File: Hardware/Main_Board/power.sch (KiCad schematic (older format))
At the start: 5 parts

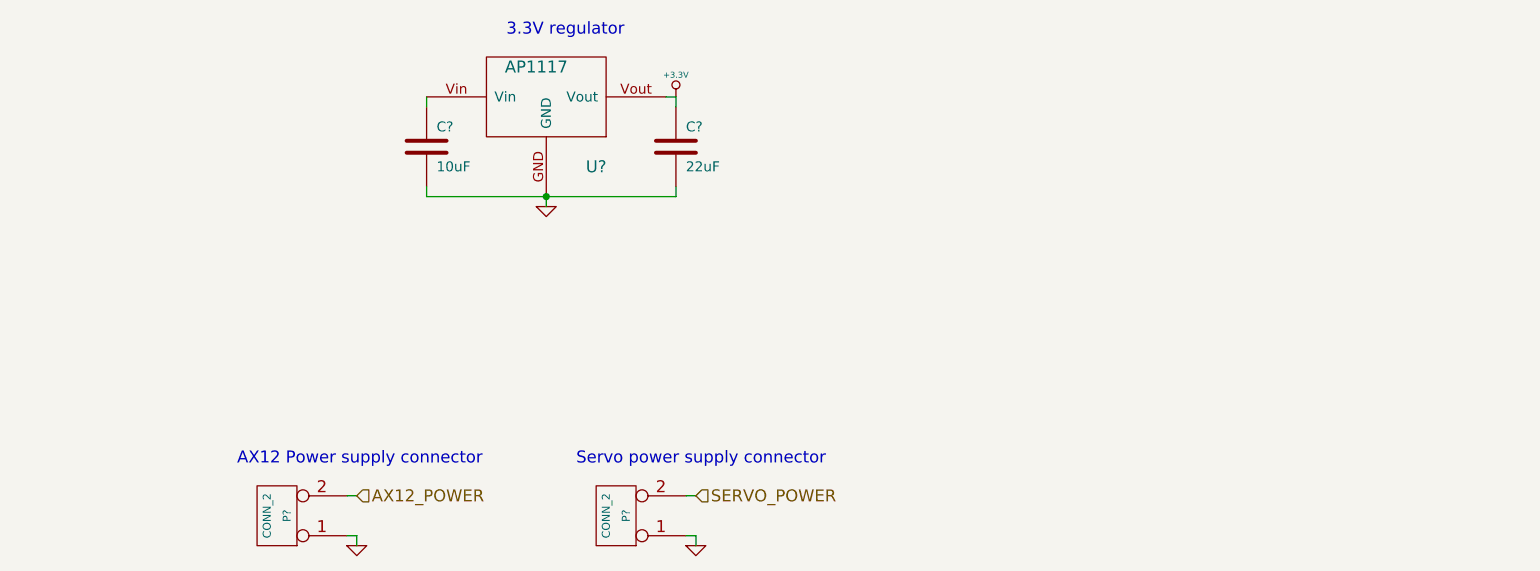
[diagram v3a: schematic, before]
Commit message: [HARDWARE] Finish motor interface and add SWD interface
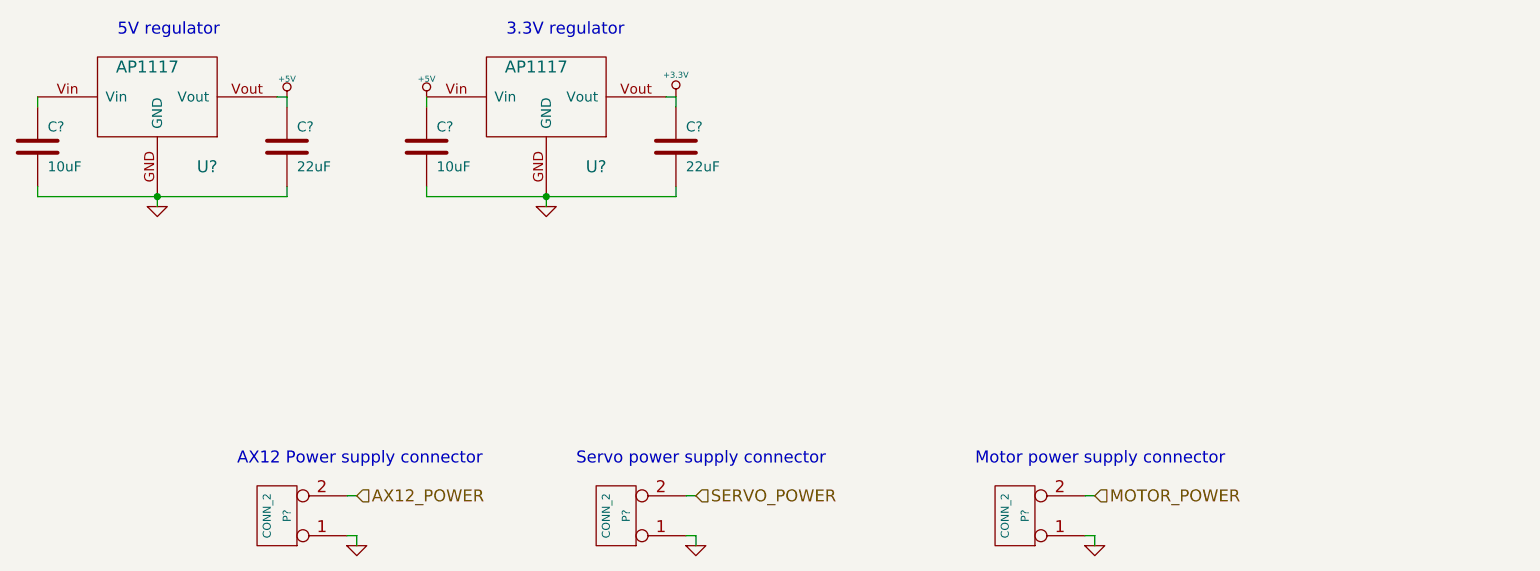
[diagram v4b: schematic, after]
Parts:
- added C?: 10uF, symbol C
- added C?: 22uF, symbol C
- added P?: CONN_2, symbol CONN_2
- added U?: AP1117, symbol AP1117
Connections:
- net GND: now also C?.2, C?.2, P?.1 (P1), U?.GND
- net +5V: now reaches C?.1, U?.Vin
- net +5V: now also C?.1, U?.Vout
- new net: C?.1, U?.Vin
- new net MOTOR_POWER: P?.2 (PM)
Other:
- note added: "5V regulator"
- note added: "Motor power supply connector"
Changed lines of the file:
@@
-EESchema Schematic File Version 2  date mer. 09 oct. 2013 08:53:10 CEST
+EESchema Schematic File Version 2  date mer. 09 oct. 2013 21:01:20 CEST
 LIBS:power
 LIBS:device
@@
 LIBS:sd_holder
 LIBS:ap1117
+LIBS:l298
 LIBS:ausbee-cache
 EELAYER 25  0
@@
 $Descr A4 11700 8267
 encoding utf-8
-Sheet 2 5
+Sheet 4 6
 Title ""
 Date "9 oct 2013"
@@
 Comment4 ""
 $EndDescr
+Text Notes 6250 4650 0    60   ~ 0
+Motor power supply connector
+Wire Wire Line
+	6850 4800 6800 4800
+Wire Wire Line
+	6850 5050 6850 5000
+Wire Wire Line
+	6850 5000 6800 5000
+Text HLabel 6850 4800 2    60   Input ~ 0
+MOTOR_POWER
+$Comp
+L GND #PWR?
+U 1 1 52558D99
+P 6850 5050
+F 0 "#PWR?" H 6850 5050 30  0001 C CNN
+F 1 "GND" H 6850 4980 30  0001 C CNN
+	1    6850 5050
+	1    0    0    -1
+$EndComp
 $Comp
 L CONN_2 P?
+U 1 1 52558D98
+P 6450 4900
+F 0 "P?" V 6400 4900 40  0000 C CNN
+F 1 "CONN_2" V 6500 4900 40  0000 C CNN
+	1    6450 4900
+	-1   0    0    1
+$EndComp
+$Comp
+L +5V #PWR?
+U 1 1 52553DBF
+P 3500 2800
+F 0 "#PWR?" H 3500 2890 20  0001 C CNN
+F 1 "+5V" H 3500 2890 30  0000 C CNN
+	1    3500 2800
+	1    0    0    -1
+$EndComp
+$Comp
+L +5V #PWR?
+U 1 1 52553DB8
+P 2800 2800
+F 0 "#PWR?" H 2800 2890 20  0001 C CNN
+F 1 "+5V" H 2800 2890 30  0000 C CNN
+	1    2800 2800
+	1    0    0    -1
+$EndComp
+$Comp
+L AP1117 U?
+U 1 1 52553DB6
+P 2150 2800
+F 0 "U?" H 2400 2450 60  0000 C CNN
+F 1 "AP1117" H 2100 2950 60  0000 C CNN
+	1    2150 2800
+	1    0    0    -1
+$EndComp
+$Comp
+L GND #PWR?
+U 1 1 52553DB4
+P 2150 3350
+F 0 "#PWR?" H 2150 3350 30  0001 C CNN
+F 1 "GND" H 2150 3280 30  0001 C CNN
+	1    2150 3350
+	1    0    0    -1
+$EndComp
+$Comp
+L C C?
+U 1 1 52553DB3
+P 2800 3050
+F 0 "C?" H 2850 3150 50  0000 L CNN
+F 1 "22uF" H 2850 2950 50  0000 L CNN
+	1    2800 3050
+	1    0    0    -1
+$EndComp
+$Comp
+L C C?
+U 1 1 52553DB2
+P 1550 3050
+F 0 "C?" H 1600 3150 50  0000 L CNN
+F 1 "10uF" H 1600 2950 50  0000 L CNN
+	1    1550 3050
+	1    0    0    -1
+$EndComp
+Text Notes 1950 2500 0    60   ~ 0
+5V regulator
+Connection ~ 2150 3300
+Wire Wire Line
+	1550 3300 1550 3250
+Wire Wire Line
+	2800 3300 1550 3300
+Wire Wire Line
+	2800 2800 2800 2850
+Wire Wire Line
+	2750 2800 2800 2800
+Wire Wire Line
+	2150 3300 2150 3350
+Wire Wire Line
+	2800 3250 2800 3300
+Wire Wire Line
+	1550 2850 1550 2800
+$Comp
+L CONN_2 P?

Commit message: [HARDWARE] Complete the SWD design, remove two undrived motor interfaces
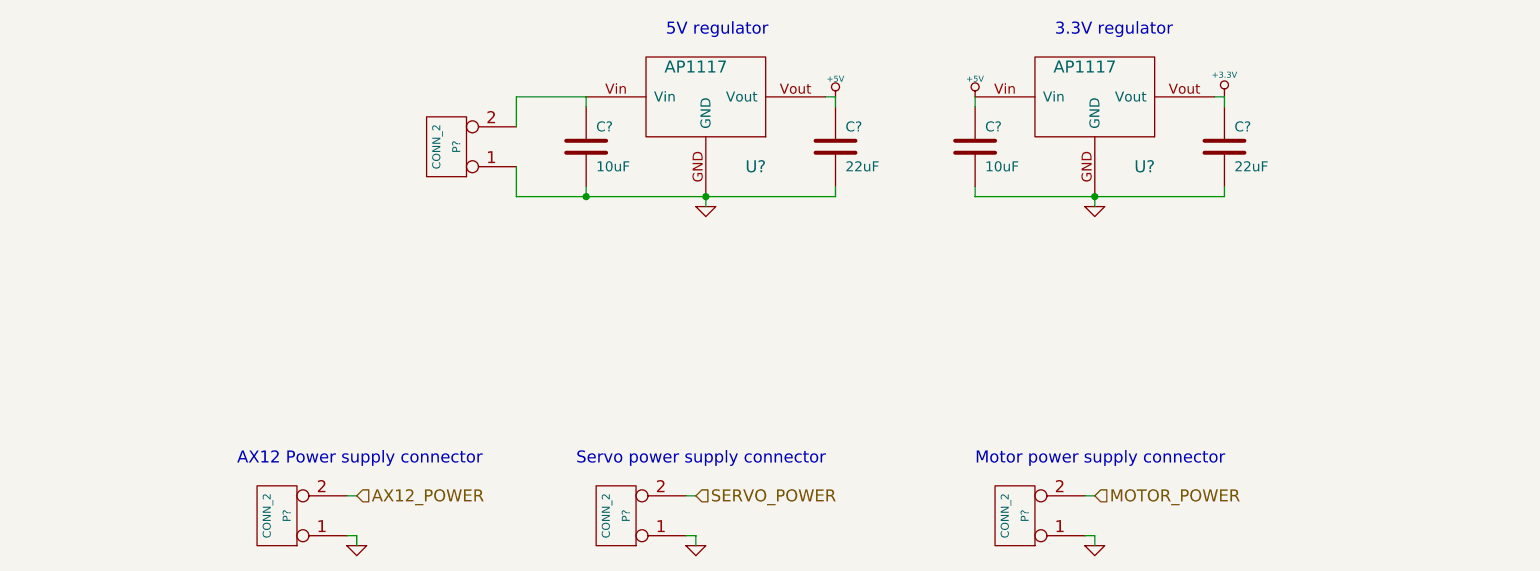
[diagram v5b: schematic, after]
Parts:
- added P?: CONN_2, symbol CONN_2
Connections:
- net GND: now also P?.1 (P1)
- net at C?.1, U?.Vin: now also P?.2 (PM)
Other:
- moved on the sheet: C?, U?
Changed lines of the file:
@@
-EESchema Schematic File Version 2  date mer. 09 oct. 2013 21:01:20 CEST
+EESchema Schematic File Version 2  date jeu. 10 oct. 2013 13:52:33 CEST
 LIBS:power
 LIBS:device
@@
 Sheet 4 6
 Title ""
-Date "9 oct 2013"
+Date "10 oct 2013"
 Rev ""
 Comp ""
@@
 Comment4 ""
 $EndDescr
+Connection ~ 4300 3300
+Wire Wire Line
+	3950 3300 5550 3300
+Wire Wire Line
+	3950 3300 3950 3150
+Wire Wire Line
+	6850 4800 6800 4800
+Wire Wire Line
+	6850 5050 6850 5000
+Wire Wire Line
+	6850 5000 6800 5000
+Connection ~ 4900 3300
+Wire Wire Line
+	4300 3300 4300 3250
+Wire Wire Line
+	5550 2850 5550 2800
+Wire Wire Line
+	5550 2800 5500 2800
+Wire Wire Line
+	4900 3300 4900 3350
+Wire Wire Line
+	5550 3300 5550 3250
+Wire Wire Line
+	4300 2850 4300 2800
+Wire Wire Line
+	4800 5000 4850 5000
+Wire Wire Line
+	4850 5000 4850 5050
+Wire Wire Line
+	4850 4800 4800 4800
+Wire Wire Line
+	3150 4800 3100 4800
+Wire Wire Line
+	6250 2850 6250 2800
+Wire Wire Line
+	7500 3250 7500 3300
+Wire Wire Line
+	6850 3300 6850 3350
+Wire Wire Line
+	7450 2800 7500 2800
+Wire Wire Line
+	7500 2800 7500 2850
+Wire Wire Line
+	7500 3300 6250 3300
+Wire Wire Line
+	6250 3300 6250 3250
+Connection ~ 6850 3300
+Wire Wire Line
+	3150 5050 3150 5000
+Wire Wire Line
+	3150 5000 3100 5000
+Wire Wire Line
+	3950 2950 3950 2800
+Wire Wire Line
+	3950 2800 4300 2800
+$Comp
+L CONN_2 P?
+U 1 1 5256944A
+P 3600 3050
+F 0 "P?" V 3550 3050 40  0000 C CNN
+F 1 "CONN_2" V 3650 3050 40  0000 C CNN
+	1    3600 3050
+	-1   0    0    1
+$EndComp
 Text Notes 6250 4650 0    60   ~ 0
 Motor power supply connector
-Wire Wire Line
-	6850 4800 6800 4800
-Wire Wire Line
-	6850 5050 6850 5000
-Wire Wire Line
-	6850 5000 6800 5000
 Text HLabel 6850 4800 2    60   Input ~ 0
 MOTOR_POWER
@@
 L +5V #PWR?
 U 1 1 52553DBF
-P 3500 2800
-F 0 "#PWR?" H 3500 2890 20  0001 C CNN
-F 1 "+5V" H 3500 2890 30  0000 C CNN
-	1    3500 2800
+P 6250 2800
+F 0 "#PWR?" H 6250 2890 20  0001 C CNN
+F 1 "+5V" H 6250 2890 30  0000 C CNN
+	1    6250 2800
 	1    0    0    -1
 $EndComp
@@
 L +5V #PWR?
 U 1 1 52553DB8
-P 2800 2800
-F 0 "#PWR?" H 2800 2890 20  0001 C CNN
-F 1 "+5V" H 2800 2890 30  0000 C CNN
-	1    2800 2800
+P 5550 2800
+F 0 "#PWR?" H 5550 2890 20  0001 C CNN
+F 1 "+5V" H 5550 2890 30  0000 C CNN
+	1    5550 2800
 	1    0    0    -1
 $EndComp
@@
 L AP1117 U?
 U 1 1 52553DB6
-P 2150 2800
-F 0 "U?" H 2400 2450 60  0000 C CNN
-F 1 "AP1117" H 2100 2950 60  0000 C CNN
-	1    2150 2800
+P 4900 2800
+F 0 "U?" H 5150 2450 60  0000 C CNN
+F 1 "AP1117" H 4850 2950 60  0000 C CNN
+	1    4900 2800
 	1    0    0    -1
 $EndComp
@@
 L GND #PWR?
 U 1 1 52553DB4
-P 2150 3350
-F 0 "#PWR?" H 2150 3350 30  0001 C CNN
-F 1 "GND" H 2150 3280 30  0001 C CNN
-	1    2150 3350
+P 4900 3350
+F 0 "#PWR?" H 4900 3350 30  0001 C CNN
+F 1 "GND" H 4900 3280 30  0001 C CNN
+	1    4900 3350
 	1    0    0    -1
 $EndComp
@@
 L C C?
 U 1 1 52553DB3
-P 2800 3050
-F 0 "C?" H 2850 3150 50  0000 L CNN
-F 1 "22uF" H 2850 2950 50  0000 L CNN
-	1    2800 3050
+P 5550 3050
+F 0 "C?" H 5600 3150 50  0000 L CNN
+F 1 "22uF" H 5600 2950 50  0000 L CNN
+	1    5550 3050
 	1    0    0    -1
 $EndComp
@@
 L C C?
 U 1 1 52553DB2
-P 1550 3050
-F 0 "C?" H 1600 3150 50  0000 L CNN
-F 1 "10uF" H 1600 2950 50  0000 L CNN
-	1    1550 3050
-	1    0    0    -1
-$EndComp
-Text Notes 1950 2500 0    60   ~ 0
+P 4300 3050
+F 0 "C?" H 4350 3150 50  0000 L CNN
+F 1 "10uF" H 4350 2950 50  0000 L CNN
+	1    4300 3050
+	1    0    0    -1
+$EndComp
+Text Notes 4700 2500 0    60   ~ 0
 5V regulator
-Connection ~ 2150 3300
-Wire Wire Line
-	1550 3300 1550 3250
-Wire Wire Line
-	2800 3300 1550 3300
-Wire Wire Line
-	2800 2800 2800 2850
-Wire Wire Line
-	2750 2800 2800 2800
-Wire Wire Line
-	2150 3300 2150 3350
-Wire Wire Line
-	2800 3250 2800 3300
-Wire Wire Line
-	1550 2850 1550 2800
 $Comp
 L CONN_2 P?
@@
 Text HLabel 4850 4800 2    60   Input ~ 0
 SERVO_POWER
-Wire Wire Line
-	4850 5000 4800 5000
-Wire Wire Line
-	4850 5050 4850 5000
-Wire Wire Line
-	4850 4800 4800 4800
 Text Notes 4250 4650 0    60   ~ 0
 Servo power supply connector
 Text Notes 2550 4650 0    60   ~ 0
 AX12 Power supply connector
-Wire Wire Line
-	3150 4800 3100 4800
-Wire Wire Line
-	3500 2850 3500 2800
-Wire Wire Line
-	4750 3250 4750 3300
-Wire Wire Line
-	4100 3300 4100 3350
-Wire Wire Line
-	4700 2800 4750 2800
-Wire Wire Line
-	4750 2800 4750 2850
-Wire Wire Line
-	4750 3300 3500 3300
-Wire Wire Line
-	3500 3300 3500 3250
-Connection ~ 4100 3300
-Wire Wire Line
-	3150 5050 3150 5000
-Wire Wire Line
-	3150 5000 3100 5000
 Text HLabel 3150 4800 2    60   Input ~ 0
 AX12_POWER
@@
 	-1   0    0    1
 $EndComp
-Text Notes 3900 2500 0    60   ~ 0
+Text Notes 6650 2500 0    60   ~ 0
 3.3V regulator
 $Comp
 L C C?
 U 1 1 52516B00
-P 3500 3050
-F 0 "C?" H 3550 3150 50  0000 L CNN
-F 1 "10uF" H 3550 2950 50  0000 L CNN
-	1    3500 3050
+P 6250 3050
+F 0 "C?" H 6300 3150 50  0000 L CNN
+F 1 "10uF" H 6300 2950 50  0000 L CNN
+	1    6250 3050
 	1    0    0    -1
 $EndComp
@@
 L C C?
 U 1 1 52516AF5
-P 4750 3050
-F 0 "C?" H 4800 3150 50  0000 L CNN
-F 1 "22uF" H 4800 2950 50  0000 L CNN
-	1    4750 3050
+P 7500 3050
+F 0 "C?" H 7550 3150 50  0000 L CNN
+F 1 "22uF" H 7550 2950 50  0000 L CNN
+	1    7500 3050
 	1    0    0    -1
 $EndComp
@@
 L GND #PWR?
 U 1 1 52516AEA
-P 4100 3350
-F 0 "#PWR?" H 4100 3350 30  0001 C CNN
-F 1 "GND" H 4100 3280 30  0001 C CNN
-	1    4100 3350
+P 6850 3350
+F 0 "#PWR?" H 6850 3350 30  0001 C CNN
+F 1 "GND" H 6850 3280 30  0001 C CNN
+	1    6850 3350
 	1    0    0    -1
 $EndComp
@@
 L +3.3V #PWR?
 U 1 1 52516ADF
-P 4750 2800
-F 0 "#PWR?" H 4750 2760 30  0001 C CNN
-F 1 "+3.3V" H 4750 2910 30  0000 C CNN
-	1    4750 2800
+P 7500 2800
+F 0 "#PWR?" H 7500 2760 30  0001 C CNN
+F 1 "+3.3V" H 7500 2910 30  0000 C CNN
+	1    7500 2800
 	1    0    0    -1
 $EndComp
@@
 L AP1117 U?
 U 1 1 52516AB1
-P 4100 2800
-F 0 "U?" H 4350 2450 60  0000 C CNN
-F 1 "AP1117" H 4050 2950 60  0000 C CNN
-	1    4100 2800
-	1    0    0    -1
-$EndComp
+P 6850 2800
+F 0 "U?" H 7100 2450 60  0000 C CNN
+F 1 "AP1117" H 6800 2950 60  0000 C CNN
+	1    6850 2800
+	1    0    0    -1
+$EndComp

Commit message: [HARDWARE] Component association + schematic modifications
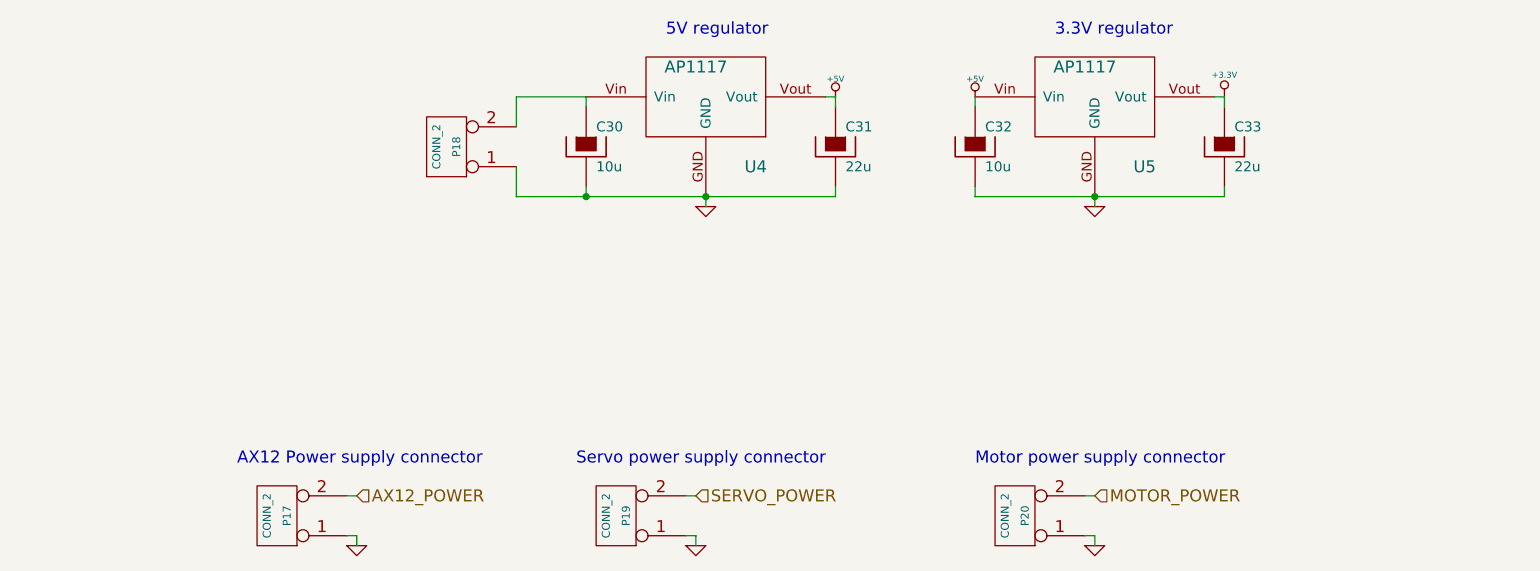
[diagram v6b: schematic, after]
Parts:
- removed C? (x2): 22uF, symbol C
- removed C? (x2): 10uF, symbol C
- added C30, C32: 10u, symbol CP
- added C31, C33: 22u, symbol CP
- gave numbers to parts that had none: 6
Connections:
- net +3.3V: now also C33.1
- net +5V: now also C31.1, C32.1
- net GND: now also C30.2, C31.2, C32.2, C33.2
- net at P18.2 (PM), U4.Vin: now also C30.1
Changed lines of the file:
@@
-EESchema Schematic File Version 2  date jeu. 10 oct. 2013 13:52:33 CEST
+EESchema Schematic File Version 2  date mer. 16 oct. 2013 19:37:53 CEST
 LIBS:power
 LIBS:device
@@
 LIBS:ap1117
 LIBS:l298
+LIBS:conn_4_jst
+LIBS:conn_2_jst
+LIBS:microsd_holder
 LIBS:ausbee-cache
 EELAYER 25  0
@@
 Sheet 4 6
 Title ""
-Date "10 oct 2013"
+Date "16 oct 2013"
 Rev ""
 Comp ""
@@
 Comment4 ""
 $EndDescr
+$Comp
+L CP C33
+U 1 1 525AC994
+P 7500 3050
+F 0 "C33" H 7550 3150 50  0000 L CNN
+F 1 "22u" H 7550 2950 50  0000 L CNN
+	1    7500 3050
+	1    0    0    -1
+$EndComp
+$Comp
+L CP C32
+U 1 1 525AC981
+P 6250 3050
+F 0 "C32" H 6300 3150 50  0000 L CNN
+F 1 "10u" H 6300 2950 50  0000 L CNN
+	1    6250 3050
+	1    0    0    -1
+$EndComp
+$Comp
+L CP C31
+U 1 1 525AC973
+P 5550 3050
+F 0 "C31" H 5600 3150 50  0000 L CNN
+F 1 "22u" H 5600 2950 50  0000 L CNN
+	1    5550 3050
+	1    0    0    -1
+$EndComp
+$Comp
+L CP C30
+U 1 1 525AC95F
+P 4300 3050
+F 0 "C30" H 4350 3150 50  0000 L CNN
+F 1 "10u" H 4350 2950 50  0000 L CNN
+	1    4300 3050
+	1    0    0    -1
+$EndComp
 Connection ~ 4300 3300
 Wire Wire Line
@@
 	3950 2800 4300 2800
 $Comp
-L CONN_2 P?
+L CONN_2 P18
 U 1 1 5256944A
 P 3600 3050
-F 0 "P?" V 3550 3050 40  0000 C CNN
+F 0 "P18" V 3550 3050 40  0000 C CNN
 F 1 "CONN_2" V 3650 3050 40  0000 C CNN
 	1    3600 3050
@@
 MOTOR_POWER
 $Comp
-L GND #PWR?
+L GND #PWR141
 U 1 1 52558D99
 P 6850 5050
-F 0 "#PWR?" H 6850 5050 30  0001 C CNN
+F 0 "#PWR141" H 6850 5050 30  0001 C CNN
 F 1 "GND" H 6850 4980 30  0001 C CNN
 	1    6850 5050
@@
 $EndComp
 $Comp
-L CONN_2 P?
+L CONN_2 P20
 U 1 1 52558D98
 P 6450 4900
-F 0 "P?" V 6400 4900 40  0000 C CNN
+F 0 "P20" V 6400 4900 40  0000 C CNN
 F 1 "CONN_2" V 6500 4900 40  0000 C CNN
 	1    6450 4900
@@
 $EndComp
 $Comp
-L +5V #PWR?
+L +5V #PWR139
 U 1 1 52553DBF
 P 6250 2800
-F 0 "#PWR?" H 6250 2890 20  0001 C CNN
+F 0 "#PWR139" H 6250 2890 20  0001 C CNN
 F 1 "+5V" H 6250 2890 30  0000 C CNN
 	1    6250 2800
@@
 $EndComp
 $Comp
-L +5V #PWR?
+L +5V #PWR138
 U 1 1 52553DB8
 P 5550 2800
-F 0 "#PWR?" H 5550 2890 20  0001 C CNN
+F 0 "#PWR138" H 5550 2890 20  0001 C CNN
 F 1 "+5V" H 5550 2890 30  0000 C CNN
 	1    5550 2800
@@
 $EndComp
 $Comp
-L AP1117 U?
+L AP1117 U4
 U 1 1 52553DB6
 P 4900 2800
-F 0 "U?" H 5150 2450 60  0000 C CNN
+F 0 "U4" H 5150 2450 60  0000 C CNN
 F 1 "AP1117" H 4850 2950 60  0000 C CNN
 	1    4900 2800
@@
 $EndComp
 $Comp
-L GND #PWR?
+L GND #PWR137
 U 1 1 52553DB4
 P 4900 3350
-F 0 "#PWR?" H 4900 3350 30  0001 C CNN
+F 0 "#PWR137" H 4900 3350 30  0001 C CNN
 F 1 "GND" H 4900 3280 30  0001 C CNN
 	1    4900 3350
 	1    0    0    -1
 $EndComp
-$Comp
-L C C?
-U 1 1 52553DB3
-P 5550 3050
-F 0 "C?" H 5600 3150 50  0000 L CNN
-F 1 "22uF" H 5600 2950 50  0000 L CNN
-	1    5550 3050
-	1    0    0    -1
-$EndComp
-$Comp
-L C C?
-U 1 1 52553DB2
-P 4300 3050
-F 0 "C?" H 4350 3150 50  0000 L CNN
-F 1 "10uF" H 4350 2950 50  0000 L CNN
-	1    4300 3050
-	1    0    0    -1
-$EndComp
 Text Notes 4700 2500 0    60   ~ 0
 5V regulator
 $Comp
-L CONN_2 P?
+L CONN_2 P19
 U 1 1 52543C3C
 P 4450 4900
-F 0 "P?" V 4400 4900 40  0000 C CNN
+F 0 "P19" V 4400 4900 40  0000 C CNN
 F 1 "CONN_2" V 4500 4900 40  0000 C CNN
 	1    4450 4900
@@
 $EndComp
 $Comp
-L GND #PWR?
+L GND #PWR136
 U 1 1 52543C3B
 P 4850 5050
-F 0 "#PWR?" H 4850 5050 30  0001 C CNN
+F 0 "#PWR136" H 4850 5050 30  0001 C CNN
 F 1 "GND" H 4850 4980 30  0001 C CNN
 	1    4850 5050
@@
 AX12_POWER
 $Comp
-L GND #PWR?
+L GND #PWR135
 U 1 1 525198A8
 P 3150 5050
-F 0 "#PWR?" H 3150 5050 30  0001 C CNN
+F 0 "#PWR135" H 3150 5050 30  0001 C CNN
 F 1 "GND" H 3150 4980 30  0001 C CNN
 	1    3150 5050
@@
 $EndComp
 $Comp
-L CONN_2 P?
+L CONN_2 P17
 U 1 1 5251989A
 P 2750 4900
-F 0 "P?" V 2700 4900 40  0000 C CNN
+F 0 "P17" V 2700 4900 40  0000 C CNN
 F 1 "CONN_2" V 2800 4900 40  0000 C CNN
 	1    2750 4900
@@
 3.3V regulator
 $Comp
-L C C?
-U 1 1 52516B00
-P 6250 3050
-F 0 "C?" H 6300 3150 50  0000 L CNN
-F 1 "10uF" H 6300 2950 50  0000 L CNN
-	1    6250 3050
-	1    0    0    -1
-$EndComp
-$Comp
-L C C?
-U 1 1 52516AF5
-P 7500 3050
-F 0 "C?" H 7550 3150 50  0000 L CNN
-F 1 "22uF" H 7550 2950 50  0000 L CNN
-	1    7500 3050
-	1    0    0    -1
-$EndComp
-$Comp
-L GND #PWR?
+L GND #PWR140
 U 1 1 52516AEA
 P 6850 3350
-F 0 "#PWR?" H 6850 3350 30  0001 C CNN
+F 0 "#PWR140" H 6850 3350 30  0001 C CNN
 F 1 "GND" H 6850 3280 30  0001 C CNN
 	1    6850 3350
@@
 $EndComp
 $Comp
-L +3.3V #PWR?
+L +3.3V #PWR142
 U 1 1 52516ADF
 P 7500 2800
-F 0 "#PWR?" H 7500 2760 30  0001 C CNN
+F 0 "#PWR142" H 7500 2760 30  0001 C CNN
 F 1 "+3.3V" H 7500 2910 30  0000 C CNN
 	1    7500 2800
@@
 $EndComp
 $Comp
-L AP1117 U?
+L AP1117 U5
 U 1 1 52516AB1
 P 6850 2800
-F 0 "U?" H 7100 2450 60  0000 C CNN
+F 0 "U5" H 7100 2450 60  0000 C CNN
 F 1 "AP1117" H 6800 2950 60  0000 C CNN
 	1    6850 2800
